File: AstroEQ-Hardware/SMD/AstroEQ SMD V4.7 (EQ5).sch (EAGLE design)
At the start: 53 parts, among them IC1 ATMEGA162-16AU, IC2 PIC18F14K50-I/SS, IC3 78L05, J1 POWER_JACKPANEL, M1 Motor Driver, M2 Motor Driver, Q1 NTR4501NT1G, X1 16MHz, X2 12MHz

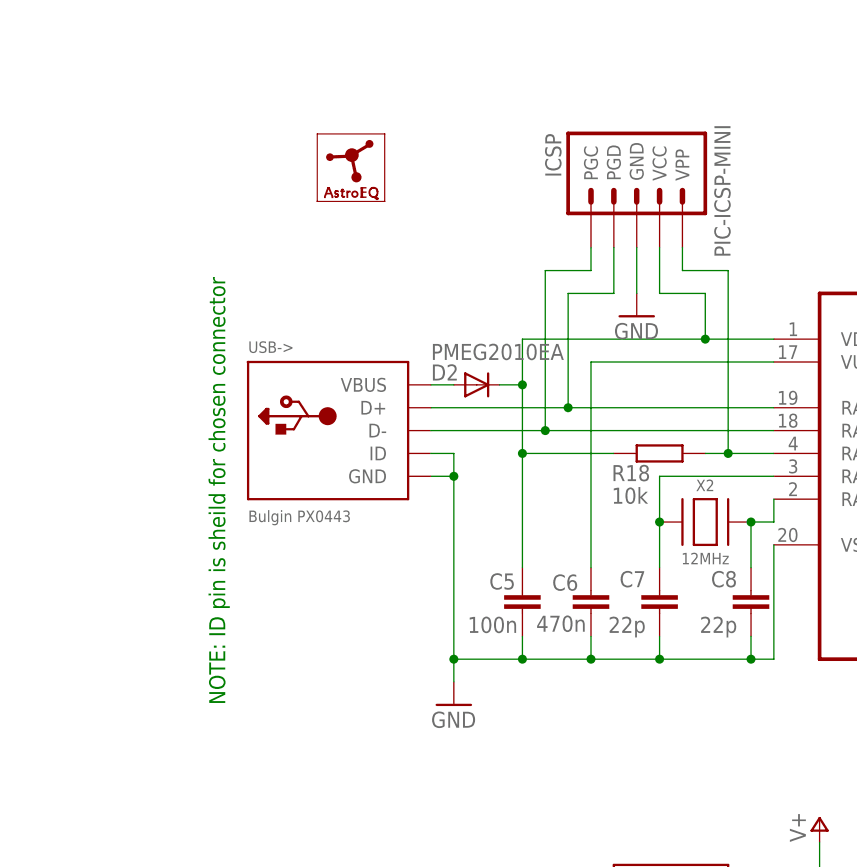
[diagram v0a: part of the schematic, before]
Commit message: Update Hardware Designs
Minor corrections to part attributes and some components in the V4.7
design moved slightly to avoid collisions as found during the prototype
build.
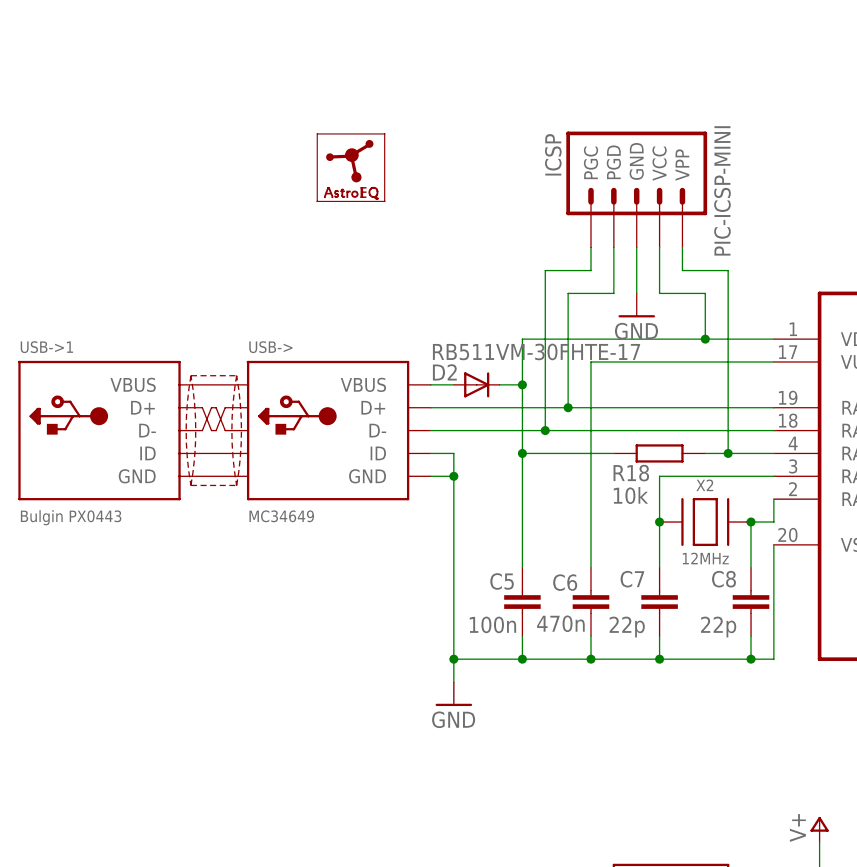
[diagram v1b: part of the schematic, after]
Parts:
- D2: value PMEG2010EA -> RB511VM-30FHTE-17; MF NEXPERIA -> ROHM; MPN PMEG2010EA -> RB511VM-30FHTE-17; OC_FARNELL 8737908 -> 2581544
- USB->: value Bulgin PX0443 -> MC34649; MF BULGIN -> MULTICOMP; MPN PX0443 -> MC34649; OC_FARNELL 1229685 -> 1675777
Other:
- note removed: "NOTE: ID pin is sheild for chosen connector"
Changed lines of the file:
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@@
 <grid distance="0.1" unitdist="inch" unit="inch" style="lines" multiple="1" display="no" altdistance="0.01" altunitdist="inch" altunit="inch"/>
 <layers>
-<layer number="1" name="Top" color="4" fill="1" visible="no" active="no"/>
-<layer number="2" name="Route2" color="1" fill="3" visible="no" active="no"/>
-<layer number="3" name="Route3" color="4" fill="3" visible="no" active="no"/>
-<layer number="14" name="Route14" color="1" fill="6" visible="no" active="no"/>
-<layer number="15" name="Route15" color="4" fill="6" visible="no" active="no"/>
-<layer number="16" name="Bottom" color="1" fill="1" visible="no" active="no"/>
-<layer number="17" name="Pads" color="2" fill="1" visible="no" active="no"/>
-<layer number="18" name="Vias" color="2" fill="1" visible="no" active="no"/>
-<layer number="19" name="Unrouted" color="6" fill="1" visible="no" active="no"/>
-<layer number="20" name="Dimension" color="15" fill="1" visible="no" active="no"/>
-<layer number="21" name="tPlace" color="7" fill="1" visible="no" active="no"/>
-<layer number="22" name="bPlace" color="7" fill="1" visible="no" active="no"/>
-<layer number="23" name="tOrigins" color="15" fill="1" visible="no" active="no"/>
-<layer number="24" name="bOrigins" color="15" fill="1" visible="no" active="no"/>
-<layer number="25" name="tNames" color="15" fill="1" visible="no" active="no"/>
-<layer number="26" name="bNames" color="7" fill="1" visible="no" active="no"/>
-<layer number="27" name="tValues" color="15" fill="1" visible="no" active="no"/>
-<layer number="28" name="bValues" color="7" fill="1" visible="no" active="no"/>
+<layer number="1" name="Top" color="4" fill="1" visible="yes" active="no"/>
+<layer number="2" name="Route2" color="1" fill="3" visible="yes" active="no"/>
+<layer number="3" name="Route3" color="4" fill="3" visible="yes" active="no"/>
+<layer number="14" name="Route14" color="1" fill="6" visible="yes" active="no"/>
+<layer number="15" name="Route15" color="4" fill="6" visible="yes" active="no"/>
+<layer number="16" name="Bottom" color="1" fill="1" visible="yes" active="no"/>
+<layer number="17" name="Pads" color="2" fill="1" visible="yes" active="no"/>
+<layer number="18" name="Vias" color="2" fill="1" visible="yes" active="no"/>
+<layer number="19" name="Unrouted" color="6" fill="1" visible="yes" active="no"/>
+<layer number="20" name="Dimension" color="15" fill="1" visible="yes" active="no"/>
+<layer number="21" name="tPlace" color="7" fill="1" visible="yes" active="no"/>
+<layer number="22" name="bPlace" color="7" fill="1" visible="yes" active="no"/>
+<layer number="23" name="tOrigins" color="15" fill="1" visible="yes" active="no"/>
+<layer number="24" name="bOrigins" color="15" fill="1" visible="yes" active="no"/>
+<layer number="25" name="tNames" color="15" fill="1" visible="yes" active="no"/>
+<layer number="26" name="bNames" color="7" fill="1" visible="yes" active="no"/>
+<layer number="27" name="tValues" color="15" fill="1" visible="yes" active="no"/>
+<layer number="28" name="bValues" color="7" fill="1" visible="yes" active="no"/>
 <layer number="29" name="tStop" color="7" fill="3" visible="no" active="no"/>
 <layer number="30" name="bStop" color="7" fill="6" visible="no" active="no"/>
@@
 <layer number="35" name="tGlue" color="7" fill="4" visible="no" active="no"/>
 <layer number="36" name="bGlue" color="7" fill="5" visible="no" active="no"/>
-<layer number="37" name="tTest" color="7" fill="1" visible="no" active="no"/>
-<layer number="38" name="bTest" color="7" fill="1" visible="no" active="no"/>
+<layer number="37" name="tTest" color="7" fill="1" visible="yes" active="no"/>
+<layer number="38" name="bTest" color="7" fill="1" visible="yes" active="no"/>
 <layer number="39" name="tKeepout" color="4" fill="11" visible="no" active="no"/>
 <layer number="40" name="bKeepout" color="1" fill="11" visible="no" active="no"/>
@@
 <layer number="44" name="Drills" color="15" fill="1" visible="no" active="no"/>
 <layer number="45" name="Holes" color="15" fill="1" visible="no" active="no"/>
-<layer number="46" name="Milling" color="3" fill="1" visible="no" active="no"/>
-<layer number="47" name="Measures" color="7" fill="1" visible="no" active="no"/>
-<layer number="48" name="Document" color="7" fill="1" visible="no" active="no"/>
-<layer number="49" name="Reference" color="7" fill="1" visible="no" active="no"/>
-<layer number="50" name="dxf" color="7" fill="1" visible="no" active="no"/>
-<layer number="51" name="tDocu" color="7" fill="1" visible="no" active="no"/>
-<layer number="52" name="bDocu" color="7" fill="1" visible="no" active="no"/>
-<layer number="53" name="tGND_GNDA" color="7" fill="9" visible="no" active="no"/>
-<layer number="54" name="bGND_GNDA" color="1" fill="9" visible="no" active="no"/>
-<layer number="56" name="wert" color="7" fill="1" visible="no" active="no"/>
-<layer number="57" name="tCAD" color="7" fill="1" visible="no" active="no"/>
-<layer number="58" name="bCAD" color="7" fill="1" visible="no" active="no"/>
-<layer number="59" name="tCarbon" color="7" fill="1" visible="no" active="no"/>
-<layer number="60" name="bCarbon" color="7" fill="1" visible="no" active="no"/>
+<layer number="46" name="Milling" color="3" fill="1" visible="yes" active="no"/>
+<layer number="47" name="Measures" color="7" fill="1" visible="yes" active="no"/>
+<layer number="48" name="Document" color="7" fill="1" visible="yes" active="no"/>
+<layer number="49" name="Reference" color="7" fill="1" visible="yes" active="no"/>
+<layer number="50" name="dxf" color="7" fill="1" visible="yes" active="no"/>
+<layer number="51" name="tDocu" color="7" fill="1" visible="yes" active="no"/>
+<layer number="52" name="bDocu" color="7" fill="1" visible="yes" active="no"/>
+<layer number="53" name="tGND_GNDA" color="7" fill="9" visible="yes" active="no"/>
+<layer number="54" name="bGND_GNDA" color="1" fill="9" visible="yes" active="no"/>
+<layer number="56" name="wert" color="7" fill="1" visible="yes" active="no"/>
+<layer number="57" name="tCAD" color="7" fill="1" visible="yes" active="no"/>
+<layer number="58" name="bCAD" color="7" fill="1" visible="yes" active="no"/>
+<layer number="59" name="tCarbon" color="7" fill="1" visible="yes" active="no"/>
+<layer number="60" name="bCarbon" color="7" fill="1" visible="yes" active="no"/>
 <layer number="90" name="Modules" color="7" fill="1" visible="yes" active="yes"/>
 <layer number="91" name="Nets" color="2" fill="1" visible="yes" active="yes"/>
@@
 </part>
 <part name="P+10" library="supply1" deviceset="+5V" device=""/>
-<part name="USB-&gt;" library="adafruit" deviceset="USB" device="BULGINWIRE" value="Bulgin PX0443">
-<attribute name="MF" value="BULGIN"/>
-<attribute name="MPN" value="PX0443"/>
-<attribute name="OC_FARNELL" value="1229685"/>
+<part name="USB-&gt;" library="adafruit" deviceset="USB" device="BULGINWIRE" value="MC34649">
+<attribute name="MF" value="MULTICOMP"/>
+<attribute name="MPN" value="MC34649"/>
+<attribute name="OC_FARNELL" value="1675777"/>
 </part>
 <part name="C6" library="rcl" deviceset="C-EU" device="C0603" value="470n">
@@
 </part>
 <part name="GND18" library="supply1" deviceset="GND" device=""/>
-<part name="D2" library="SparkFun" deviceset="DIODE" device="SOD" value="PMEG2010EA">
-<attribute name="MF" value="NEXPERIA"/>
-<attribute name="MPN" value="PMEG2010EA"/>
-<attribute name="OC_FARNELL" value="8737908"/>
+<part name="D2" library="SparkFun" deviceset="DIODE" device="SOD" value="RB511VM-30FHTE-17">
+<attribute name="MF" value="ROHM"/>
+<attribute name="MPN" value="RB511VM-30FHTE-17"/>
+<attribute name="OC_FARNELL" value="2581544"/>
 </part>
 <part name="GND19" library="supply1" deviceset="GND" device=""/>
@@
 </part>
 <part name="GND7" library="supply1" deviceset="GND" device=""/>
+<part name="USB-&gt;1" library="adafruit" deviceset="USB-PANEL" device="" value="Bulgin PX0443">
+<attribute name="MF" value="BULGIN"/>
+<attribute name="MPN" value="PX0443"/>
+<attribute name="OC_FARNELL" value="1229685"/>
+</part>
 </parts>
 <sheets>
 <sheet>
 <plain>
-<text x="-5.08" y="60.96" size="1.778" layer="91" rot="R90">NOTE: ID pin is sheild for chosen connector</text>
 <text x="452.12" y="60.96" size="1.4224" layer="97">4-contact version no longer stocked.
 Using 6-contact version with extra
@@
 </instance>
 <instance part="GND7" gate="1" x="289.56" y="114.3"/>
+<instance part="USB-&gt;1" gate="G$1" x="-17.78" y="91.44">
+<attribute name="MF" value="MOLEX" x="-17.78" y="91.44" size="1.778" layer="96" display="off"/>
+<attribute name="OC_FARNELL" x="-17.78" y="91.44" size="1.778" layer="96" display="off"/>
+<attribute name="MPN" x="-17.78" y="91.44" size="1.778" layer="96" display="off"/>
+</instance>
 </instances>
 <busses>
